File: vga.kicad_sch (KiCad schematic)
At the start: 48 parts

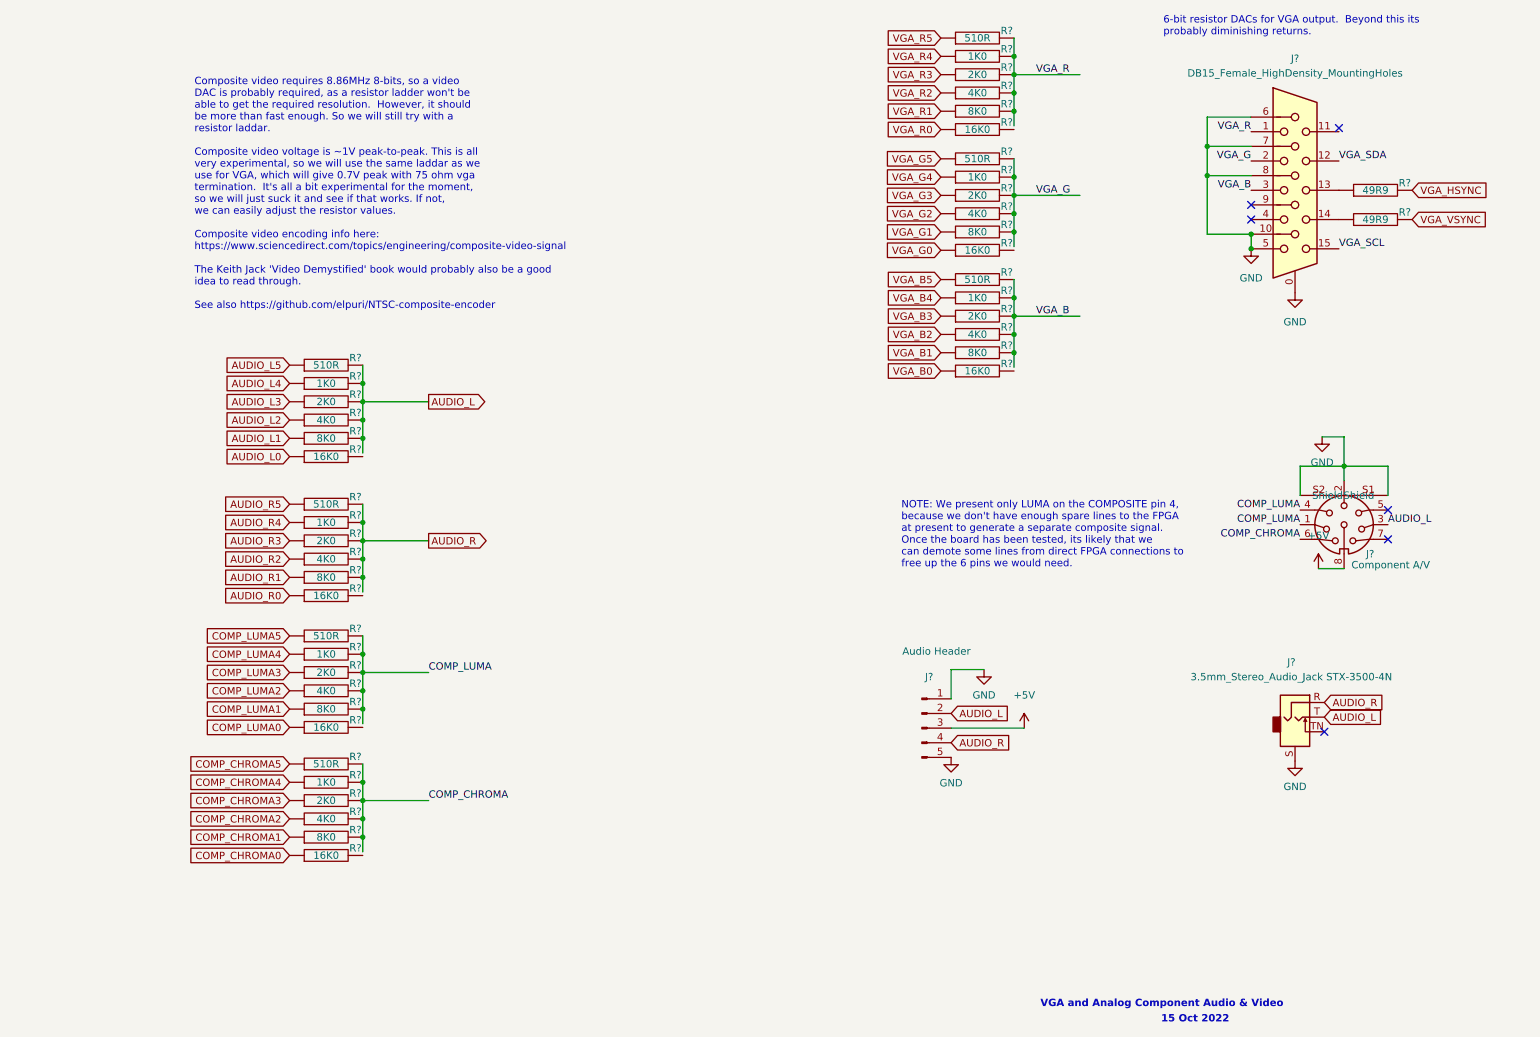
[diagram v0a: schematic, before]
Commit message: add all missing footprints
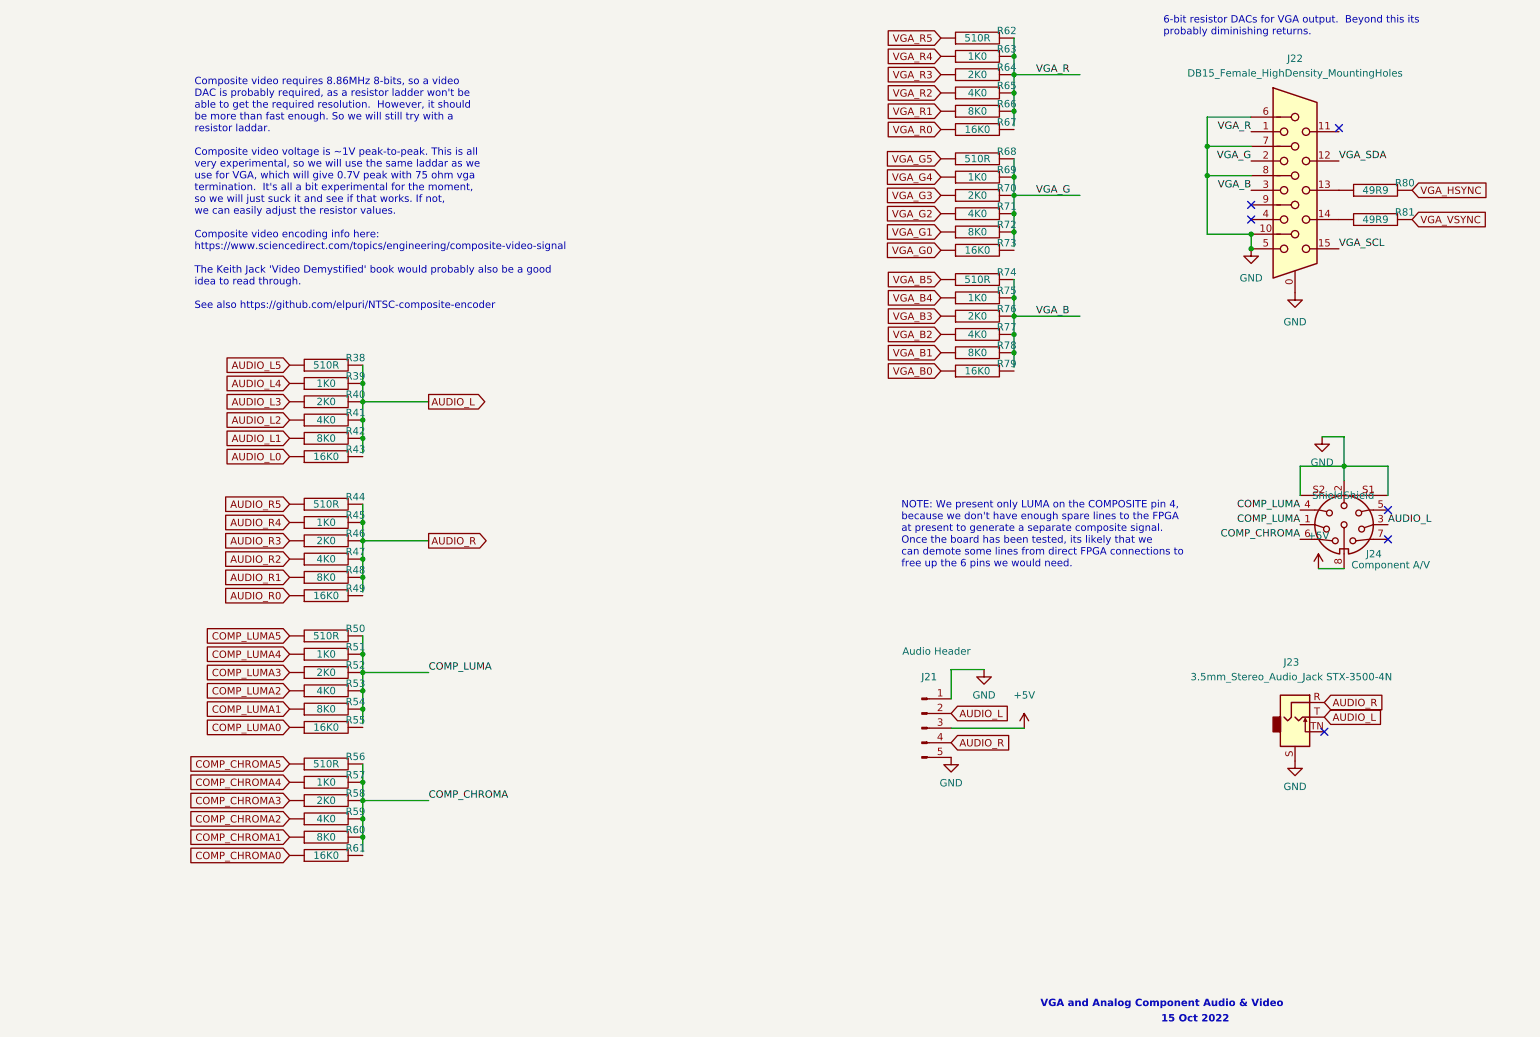
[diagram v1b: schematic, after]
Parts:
- J21: renamed from J?; footprint (none) -> Connector_PinHeader_2.54mm:PinHeader_1x05_P2.54mm_Vertical
- gave numbers to parts that had none: 47

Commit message: add C64 keyboard connector on MUX bus #9
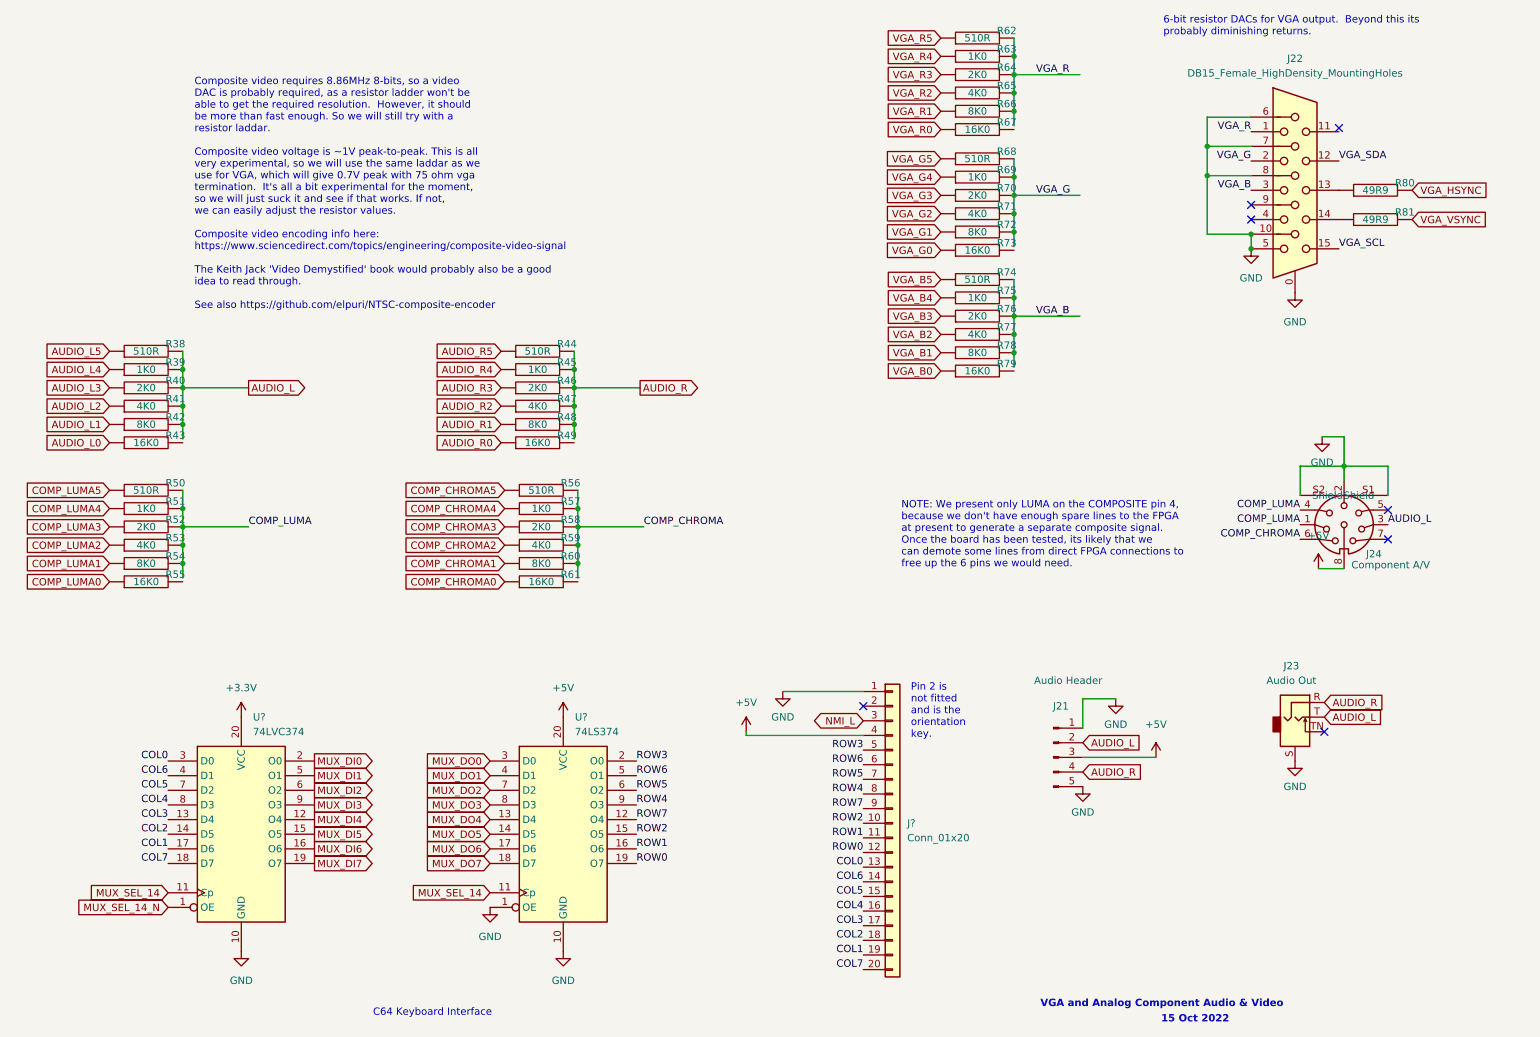
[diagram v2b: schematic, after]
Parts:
- added J?: Conn_01x20, symbol Connector_Generic:Conn_01x20
- added U?: 74LVC374, Package_DIP:DIP-20_W7.62mm, symbol 74xx:74HC374
- added U?: 74LS374, Package_DIP:DIP-20_W7.62mm, symbol 74xx:74LS374
- J23: value 3.5mm_Stereo_Audio_Jack STX-3500-4N -> Audio Out
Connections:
- net +5V: now also J?.4 (Pin_4), U?.20 (VCC)
- net GND: now also J?.1 (Pin_1), U?.1 (OE), U?.10 (GND), U?.10 (GND)
- new net +3V3: U?.20 (VCC)
- new net COL0: J?.13 (Pin_13), U?.3 (D0)
- new net COL1: J?.19 (Pin_19), U?.17 (D6)
- new net COL2: J?.18 (Pin_18), U?.14 (D5)
- new net COL3: J?.17 (Pin_17), U?.13 (D4)
- new net COL4: J?.16 (Pin_16), U?.8 (D3)
- new net COL5: J?.15 (Pin_15), U?.7 (D2)
- new net COL6: J?.14 (Pin_14), U?.4 (D1)
- new net COL7: J?.20 (Pin_20), U?.18 (D7)
- new net MUX_DI0: U?.2 (O0)
- new net MUX_DI1: U?.5 (O1)
- new net MUX_DI2: U?.6 (O2)
- new net MUX_DI3: U?.9 (O3)
- new net MUX_DI4: U?.12 (O4)
- new net MUX_DI5: U?.15 (O5)
- new net MUX_DI6: U?.16 (O6)
- new net MUX_DI7: U?.19 (O7)
- new net MUX_DO0: U?.3 (D0)
- new net MUX_DO1: U?.4 (D1)
- new net MUX_DO2: U?.7 (D2)
- new net MUX_DO3: U?.8 (D3)
- new net MUX_DO4: U?.13 (D4)
- new net MUX_DO5: U?.14 (D5)
- new net MUX_DO6: U?.17 (D6)
- new net MUX_DO7: U?.18 (D7)
- new net MUX_SEL_14: U?.11 (Cp), U?.11 (Cp)
- new net MUX_SEL_14_N: U?.1 (OE)
- new net NMI_L: J?.3 (Pin_3)
- new net ROW0: J?.12 (Pin_12), U?.19 (O7)
- new net ROW1: J?.11 (Pin_11), U?.16 (O6)
- new net ROW2: J?.10 (Pin_10), U?.15 (O5)
- new net ROW3: J?.5 (Pin_5), U?.2 (O0)
- new net ROW4: J?.8 (Pin_8), U?.9 (O3)
- new net ROW5: J?.7 (Pin_7), U?.6 (O2)
- new net ROW6: J?.6 (Pin_6), U?.5 (O1)
- new net ROW7: J?.9 (Pin_9), U?.12 (O4)
- no-connect marks 6 -> 7
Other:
- note added: "C64 Keyboard Interface"
- note added: "Pin 2 is not fitted and is the orientation key."
- moved on the sheet: J21, R38, R39, R40, R41, R42, R43, R44, R45, R46, R47, R48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

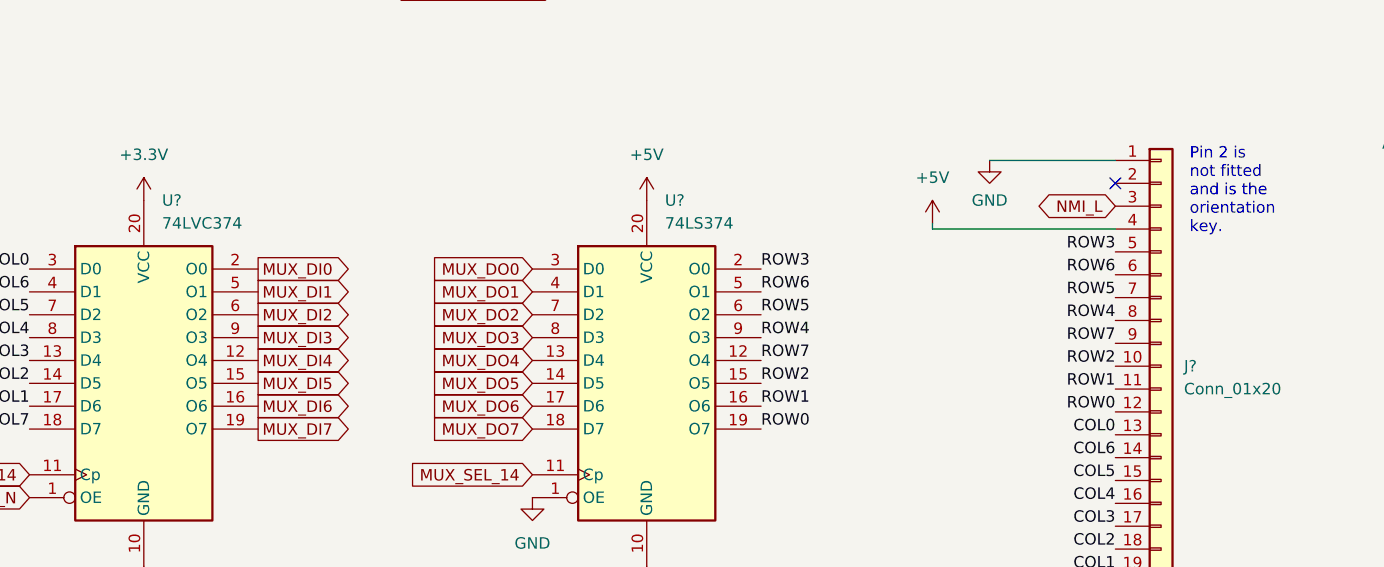
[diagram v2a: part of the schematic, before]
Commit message: place some mounting holes and reset button #3
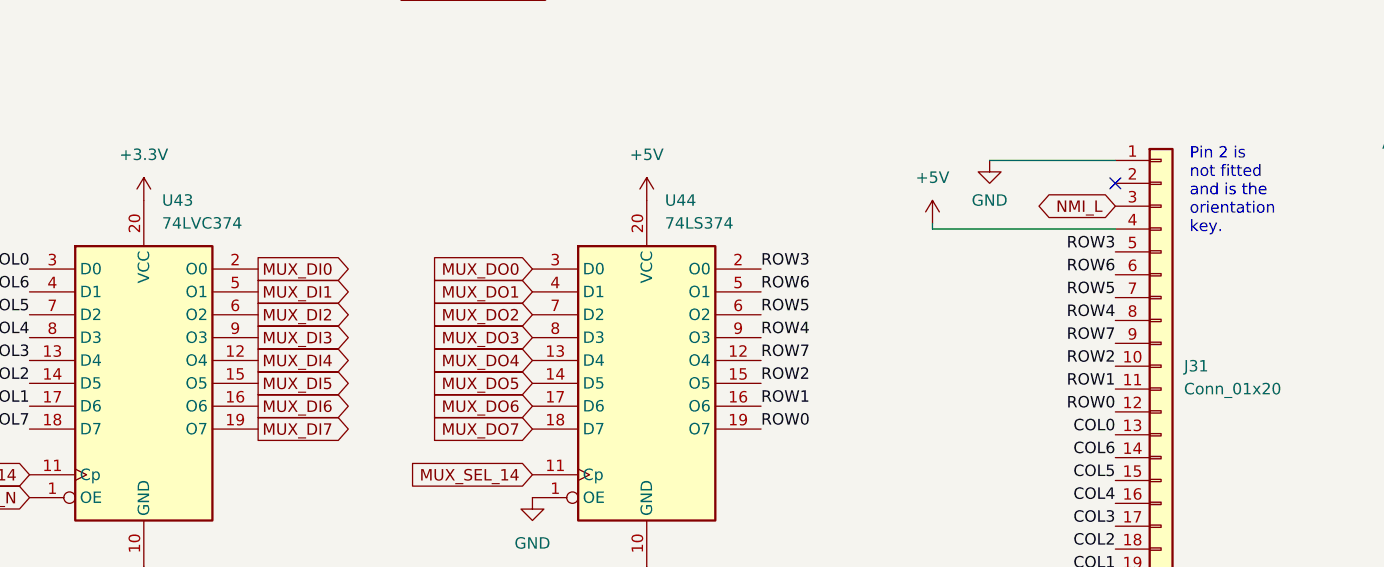
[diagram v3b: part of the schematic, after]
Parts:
- gave numbers to parts that had none: 3
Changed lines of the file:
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@@
   (symbol (lib_id "power:+3.3V") (at 53.34 140.97 0) (unit 1)
     (in_bom yes) (on_board yes) (fields_autoplaced)
-    (property "Reference" "#PWR?" (id 0) (at 53.34 144.78 0)
+    (property "Reference" "#PWR0318" (id 0) (at 53.34 144.78 0)
       (effects (font (size 1.27 1.27)) hide)
     )
@@
   (symbol (lib_id "Connector_Generic:Conn_01x20") (at 166.37 159.385 0) (unit 1)
     (in_bom yes) (on_board yes) (fields_autoplaced)
-    (property "Reference" "J?" (id 0) (at 168.91 159.3849 0)
+    (property "Reference" "J31" (id 0) (at 168.91 159.3849 0)
       (effects (font (size 1.27 1.27)) (justify left))
     )
@@
   (symbol (lib_id "power:GND") (at 109.22 181.61 0) (unit 1)
     (in_bom yes) (on_board yes) (fields_autoplaced)
-    (property "Reference" "#PWR?" (id 0) (at 109.22 187.96 0)
+    (property "Reference" "#PWR0316" (id 0) (at 109.22 187.96 0)
       (effects (font (size 1.27 1.27)) hide)
     )
@@
   (symbol (lib_id "power:GND") (at 96.52 173.99 0) (unit 1)
     (in_bom yes) (on_board yes) (fields_autoplaced)
-    (property "Reference" "#PWR?" (id 0) (at 96.52 180.34 0)
+    (property "Reference" "#PWR0315" (id 0) (at 96.52 180.34 0)
       (effects (font (size 1.27 1.27)) hide)
     )
@@
   (symbol (lib_id "power:+5V") (at 109.22 140.97 0) (unit 1)
     (in_bom yes) (on_board yes) (fields_autoplaced)
-    (property "Reference" "#PWR?" (id 0) (at 109.22 144.78 0)
+    (property "Reference" "#PWR0317" (id 0) (at 109.22 144.78 0)
       (effects (font (size 1.27 1.27)) hide)
     )
@@
   (symbol (lib_id "power:+5V") (at 140.97 143.51 0) (unit 1)
     (in_bom yes) (on_board yes) (fields_autoplaced)
-    (property "Reference" "#PWR?" (id 0) (at 140.97 147.32 0)
+    (property "Reference" "#PWR0314" (id 0) (at 140.97 147.32 0)
       (effects (font (size 1.27 1.27)) hide)
     )
@@
   (symbol (lib_id "power:GND") (at 53.34 181.61 0) (unit 1)
     (in_bom yes) (on_board yes) (fields_autoplaced)
-    (property "Reference" "#PWR?" (id 0) (at 53.34 187.96 0)
+    (property "Reference" "#PWR0319" (id 0) (at 53.34 187.96 0)
       (effects (font (size 1.27 1.27)) hide)
     )
@@
   (symbol (lib_id "power:GND") (at 147.32 136.525 0) (unit 1)
     (in_bom yes) (on_board yes) (fields_autoplaced)
-    (property "Reference" "#PWR?" (id 0) (at 147.32 142.875 0)
+    (property "Reference" "#PWR0313" (id 0) (at 147.32 142.875 0)
       (effects (font (size 1.27 1.27)) hide)
     )
@@
   (symbol (lib_id "74xx:74HC374") (at 53.34 161.29 0) (unit 1)
     (in_bom yes) (on_board yes) (fields_autoplaced)
-    (property "Reference" "U?" (id 0) (at 55.3594 140.97 0)
+    (property "Reference" "U43" (id 0) (at 55.3594 140.97 0)
       (effects (font (size 1.27 1.27)) (justify left))
     )
@@
   (symbol (lib_id "74xx:74LS374") (at 109.22 161.29 0) (unit 1)
     (in_bom yes) (on_board yes) (fields_autoplaced)
-    (property "Reference" "U?" (id 0) (at 111.2394 140.97 0)
+    (property "Reference" "U44" (id 0) (at 111.2394 140.97 0)
       (effects (font (size 1.27 1.27)) (justify left))
     )
